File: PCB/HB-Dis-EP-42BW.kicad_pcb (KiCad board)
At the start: 2 copper layers, 61.4 x 103.3 mm, 42 parts, among them J1 Reset, J2 FTDI, J3 ISP, J4 ePaper, J5 ePaper_TestPoints, J6 Supply, J7 Conn_GPIO, J8 Config, J9 Conn_I2C, Q1 IRLML6344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

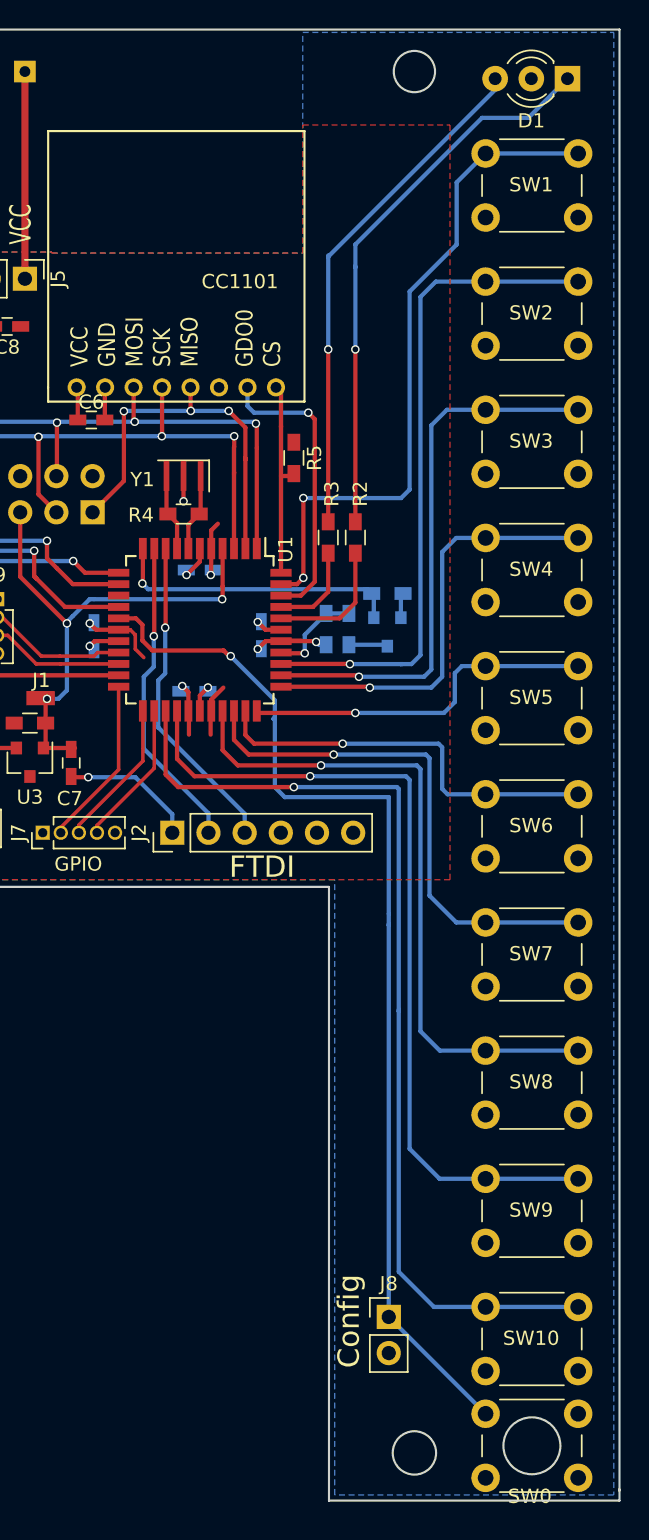
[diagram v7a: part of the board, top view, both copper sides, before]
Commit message: even more improvements on PCB
- slimmer pads on TQFP44 for easier soldering
- CC1101 power pads changed to "oval" so that the net is connected horizontal/vertical and not diagonal
- moved vias out of SMD pads
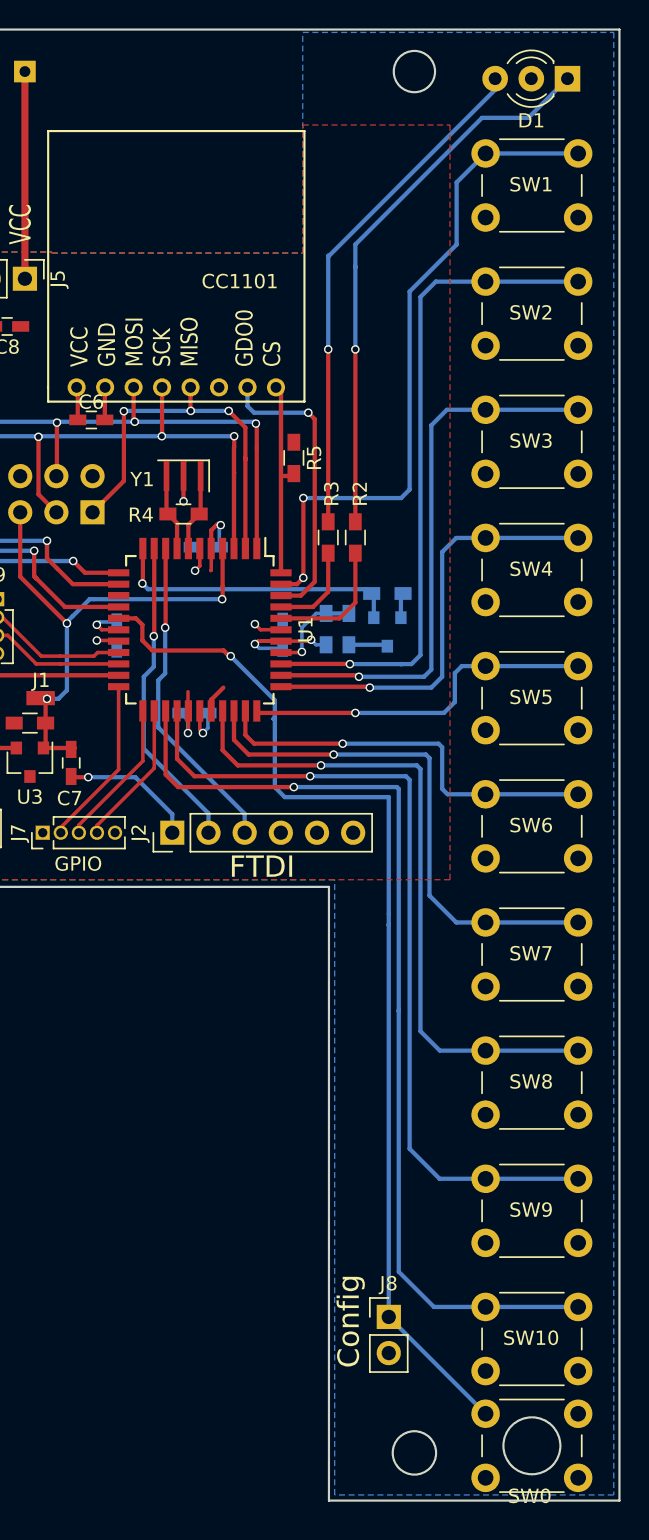
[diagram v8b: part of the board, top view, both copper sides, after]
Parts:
- U1: footprint Housings_QFP:TQFP-44_10x10mm_Pitch0.8mm -> TQFP Housings:TQFP-44_10x10mm_Pitch0.8mm_HandSoldering
- moved C2 1.66 mm to (91.4, 70.2)
- moved C3 1.60 mm to (85.1, 76.4)
- moved C4 1.54 mm to (90.6, 81.8)
- moved C5 1.50 mm to (96.8, 76.3)
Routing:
- net GND: track 41.4 -> 40.4 mm
- net VCC: track 46.3 -> 45.2 mm
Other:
- outline, holes or cut-outs redrawn
